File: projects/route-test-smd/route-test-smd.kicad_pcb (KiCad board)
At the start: 2 copper layers, 30 x 20 mm, 3 parts, among them J1 Conn_01x03

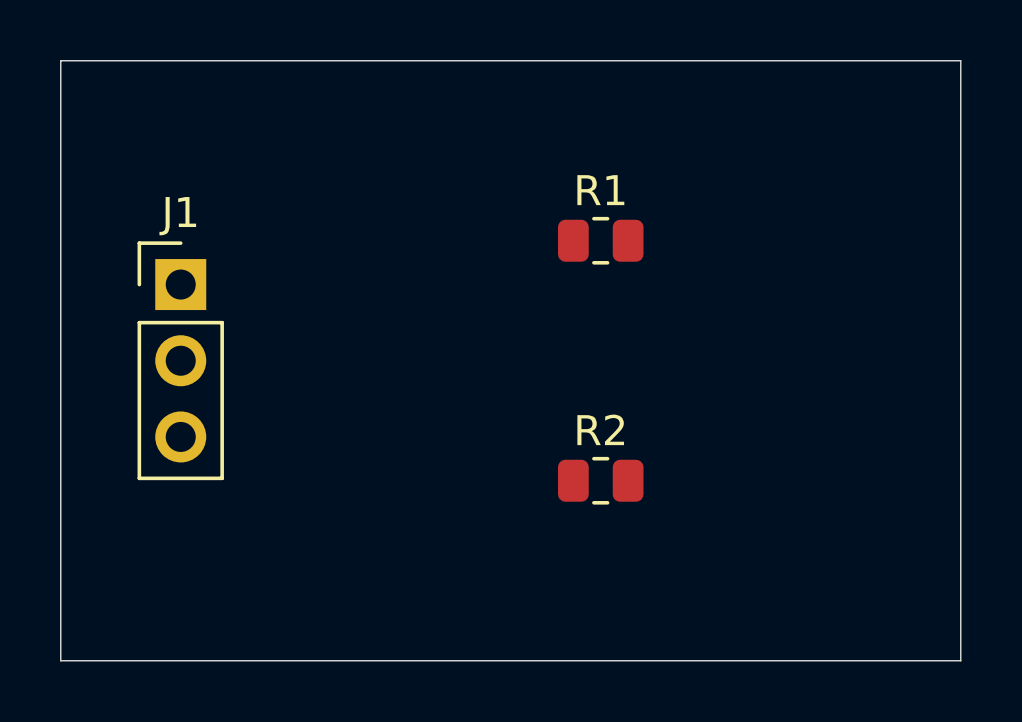
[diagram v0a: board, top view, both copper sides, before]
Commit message: route-test-smd: SES imported via KiCad GUI, saved via IPC
12 tracks, 1 via; DRC 0 unconnected. Warnings: 1 via_dangling (VIN via left
by Freerouting, F.Cu only), 2 lib_footprint_mismatch, 3 Description parity.

Co-Authored-By: Claude Opus 5.5 <noreply@anthropic.com>
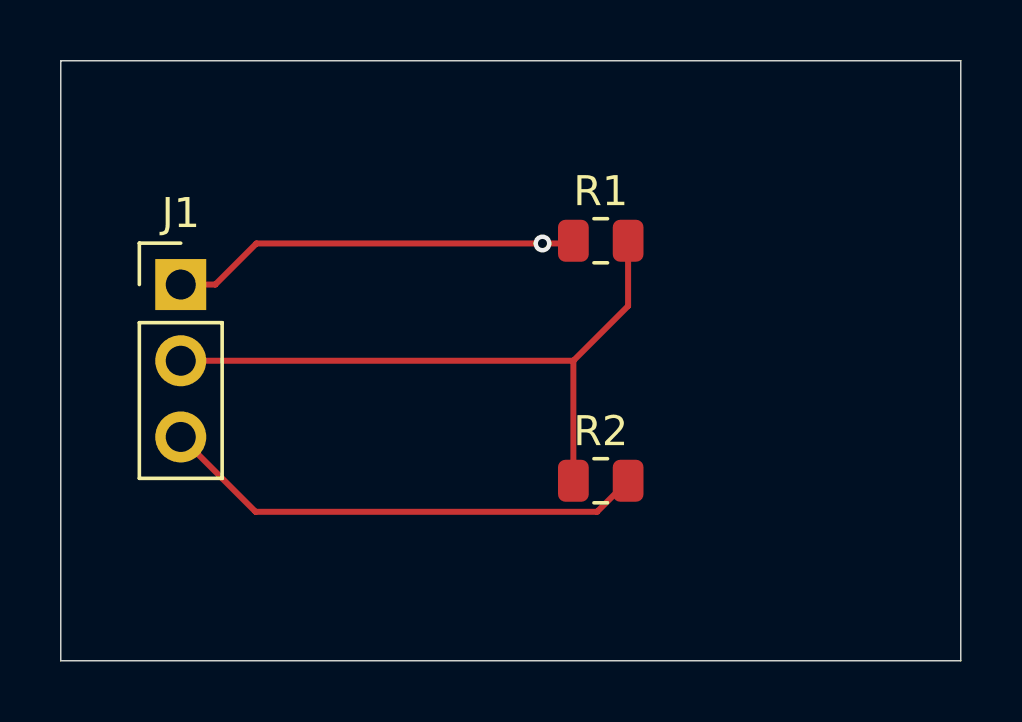
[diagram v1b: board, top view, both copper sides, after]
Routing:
- net /VOUT: track 0.00 -> 21.8 mm
- net /GND: track 0.00 -> 16.4 mm
- net /VIN: track 0.00 -> 13.7 mm, vias 0 -> 1
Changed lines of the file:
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@@
 		(layer "Edge.Cuts")
+	)
+	(segment
+		(start 116.997 106.0905)
+		(end 117.0875 106)
+		(width 0.2)
+		(layer "F.Cu")
+		(net "/VIN")
+	)
+	(segment
+		(start 106.5212 106.0905)
+		(end 105.1517 107.46)
+		(width 0.2)
+		(layer "F.Cu")
+		(net "/VIN")
+	)
+	(segment
+		(start 116.0572 106.0905)
+		(end 106.5212 106.0905)
+		(width 0.2)
+		(layer "F.Cu")
+		(net "/VIN")
+	)
+	(segment
+		(start 116.0572 106.0905)
+		(end 116.997 106.0905)
+		(width 0.2)
+		(layer "F.Cu")
+		(net "/VIN")
+	)
+	(segment
+		(start 104 107.46)
+		(end 105.1517 107.46)
+		(width 0.2)
+		(layer "F.Cu")
+		(net "/VIN")
+	)
+	(via
+		(at 116.0572 106.0905)
+		(size 0.6)
+		(drill 0.3)
+		(layers "F.Cu" "B.Cu")
+		(net "/VIN")
+	)
+	(segment
+		(start 118.9125 106)
+		(end 118.9125 108.175)
+		(width 0.2)
+		(layer "F.Cu")
+		(net "/VOUT")
+	)
+	(segment
+		(start 118.9125 108.175)
+		(end 117.0875 110)
+		(width 0.2)
+		(layer "F.Cu")
+		(net "/VOUT")
+	)
+	(segment
+		(start 117.0875 110)
+		(end 104 110)
+		(width 0.2)
+		(layer "F.Cu")
+		(net "/VOUT")
+	)
+	(segment
+		(start 117.0875 110)
+		(end 117.0875 114)
+		(width 0.2)
+		(layer "F.Cu")
+		(net "/VOUT")
+	)
+	(segment
+		(start 117.8772 115.0353)
+		(end 118.9125 114)
+		(width 0.2)
+		(layer "F.Cu")
+		(net "/GND")
+	)
+	(segment
+		(start 106.4953 115.0353)
+		(end 117.8772 115.0353)
+		(width 0.2)
+		(layer "F.Cu")
+		(net "/GND")
+	)
+	(segment
+		(start 104 112.54)
+		(end 106.4953 115.0353)
+		(width 0.2)
+		(layer "F.Cu")
+		(net "/GND")
 	)
 	(embedded_fonts no)
